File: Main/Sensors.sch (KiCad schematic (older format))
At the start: 11 parts, among them SW1 LEFT_BUMP, SW2 RIGHT_BUMP, U1 phototransistor, U2 phototransistor, U3 PCF8591

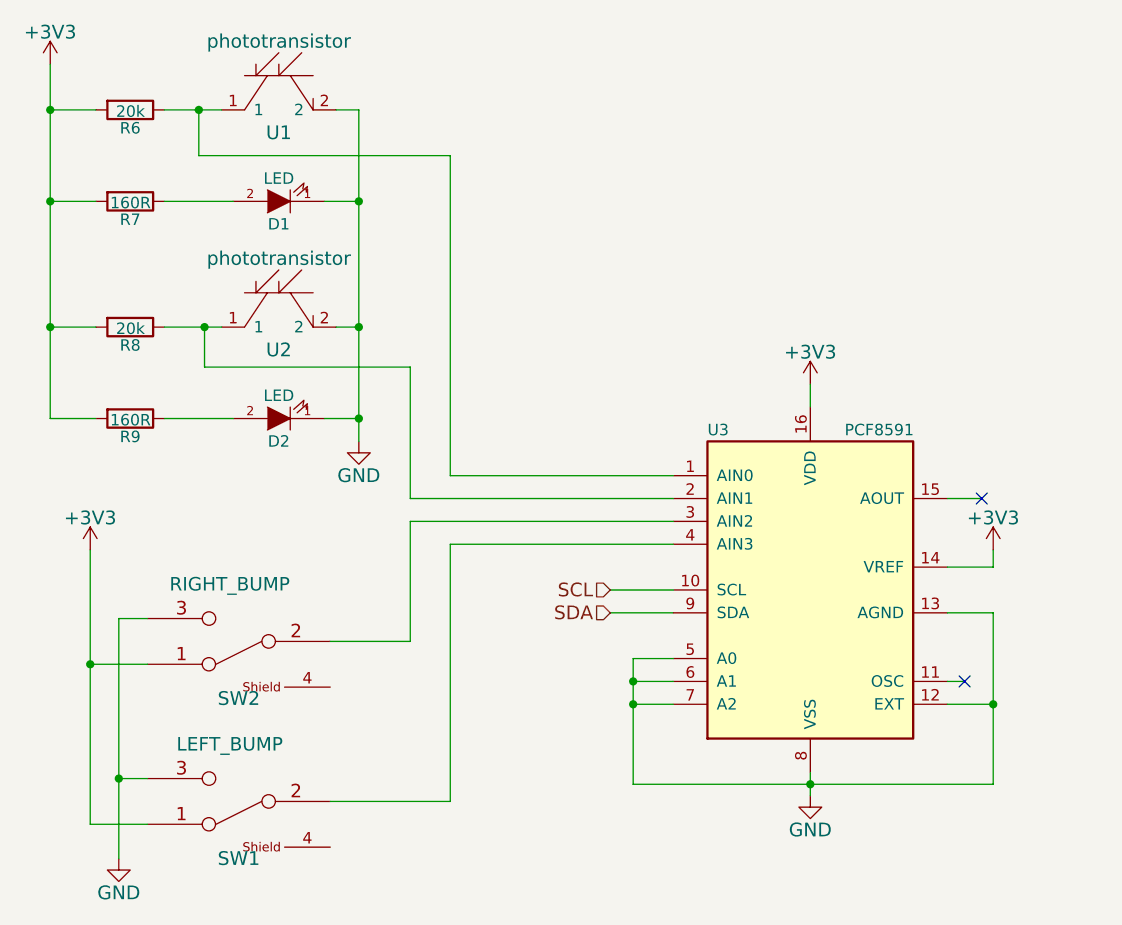
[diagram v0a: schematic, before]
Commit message: Update the BoM to embed it into KiCad
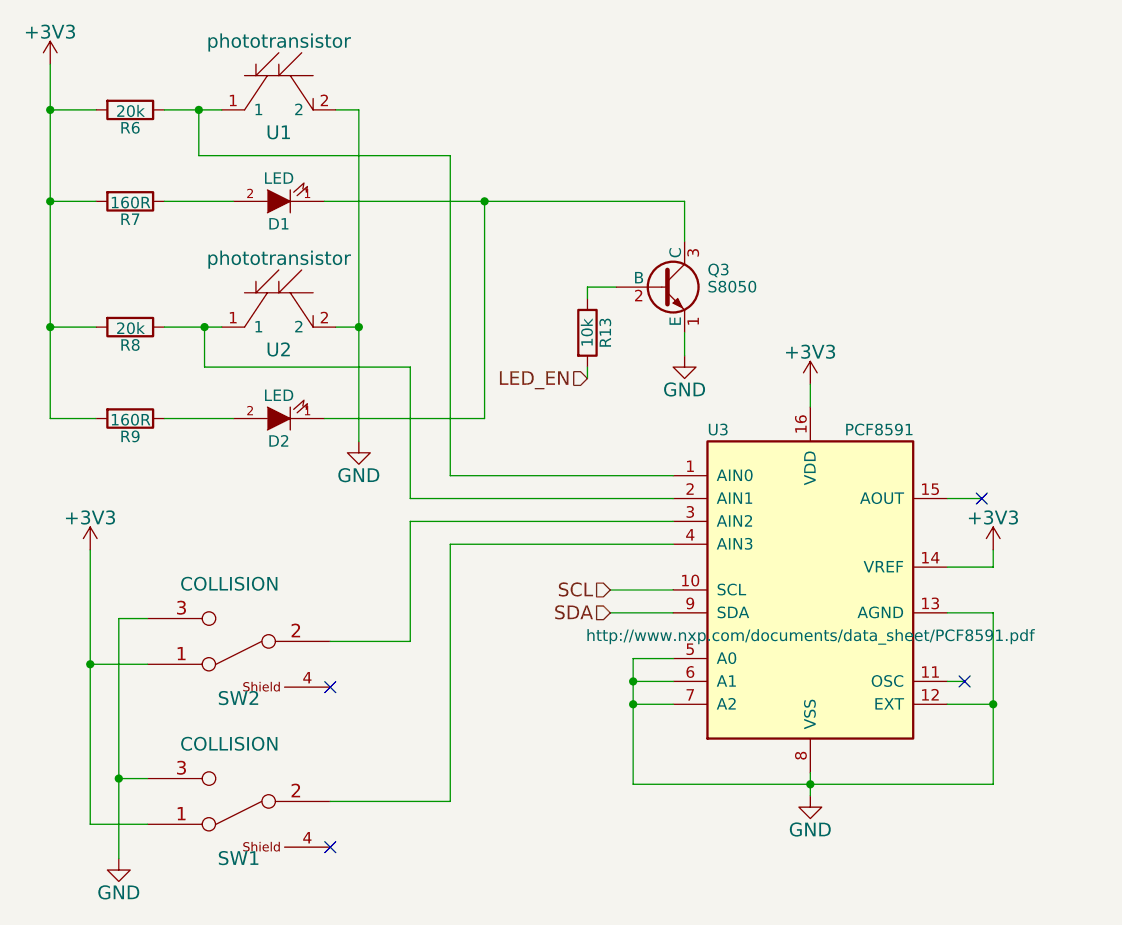
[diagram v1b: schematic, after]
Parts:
- added Q3: S8050, Custom:SOT-23, symbol S8050
- added R13: 10k, Resistors_SMD:R_0603, symbol R
- D1, D2: footprint Mirobot:SIDE-LED-REVERSED -> Custom:SIDE-LED-REVERSED; Description (none) -> Side facing SMD infrared LED; Required (none) -> y
- R6, R8: Description (none) -> 0603 20k Resistor; Manufacturer Name (MFN) (none) -> Generic; Package ID (none) -> 0603; Required (none) -> y
- R7, R9: Description (none) -> 0603 160R Resistor; Manufacturer Name (MFN) (none) -> Generic; Package ID (none) -> 0603; Required (none) -> y
- SW1: value LEFT_BUMP -> COLLISION; footprint Mirobot:LEVER_SWITCH -> Custom:LEVER_SWITCH; Description (none) -> Long lever switch; Required (none) -> y
- SW2: value RIGHT_BUMP -> COLLISION; footprint Mirobot:LEVER_SWITCH -> Custom:LEVER_SWITCH; Description (none) -> Long lever switch; Required (none) -> y
- U1, U2: footprint Mirobot:SIDE-LED -> Custom:SIDE-LED; Description (none) -> Side facing SMD infrared phototransistor; Required (none) -> y
- U3: Description (none) -> 8-Bit I2C ADC; Manfr. Part Number (MFP) (none) -> PCF8591T; Manufacturer Name (MFN) (none) -> NXP; Package ID (none) -> SO16; Required (none) -> y; Source2 (none) -> http://www.aliexpress.com/item/20pcs-lot-PCF8591T/324041985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
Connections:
- net GND: now also Q3.1 (E); no longer D1.1 (K), D2.1 (K)
- new net: D1.1 (K), D2.1 (K), Q3.3 (C)
- new net: Q3.2 (B), R13.1
- new net LED_EN: R13.2
- no-connect marks 2 -> 4
